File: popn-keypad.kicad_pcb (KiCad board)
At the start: 2 copper layers, 130.9 x 47.6 mm, 14 parts, among them U1 Arduino_Pro_Micro

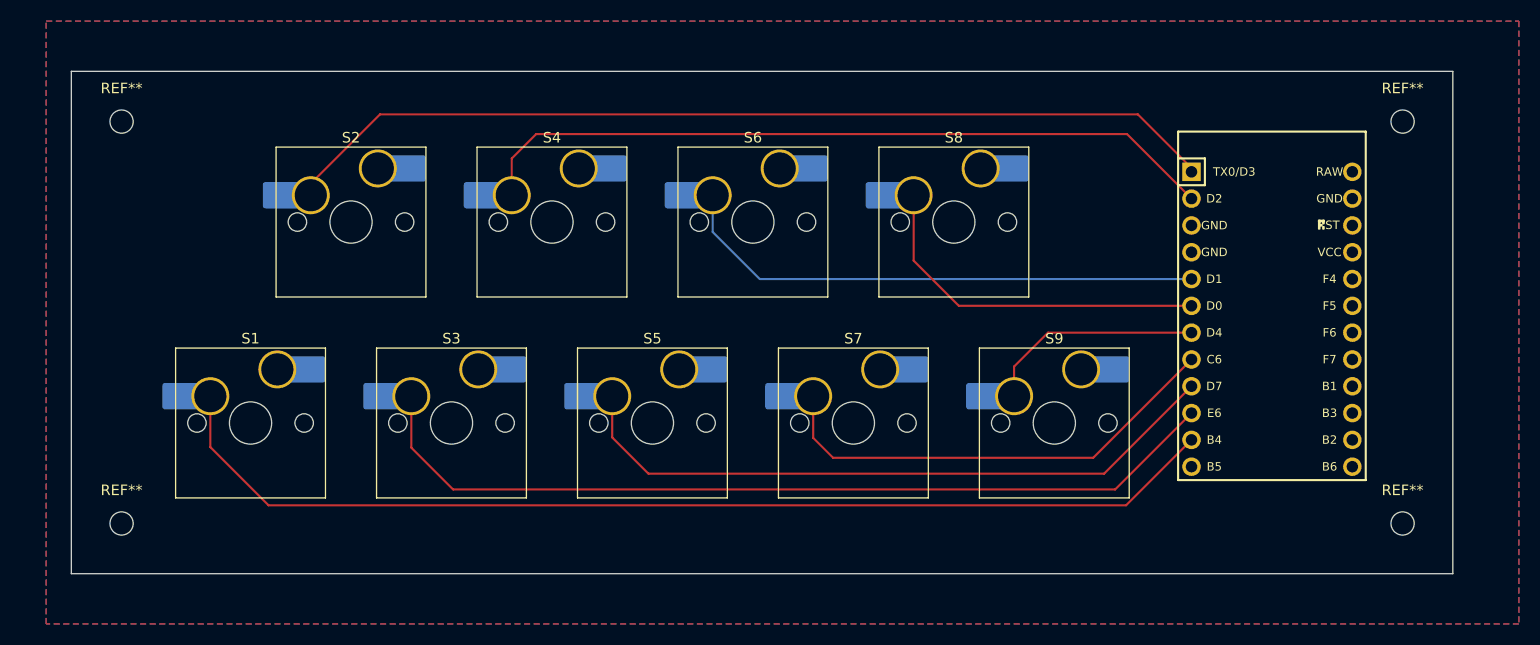
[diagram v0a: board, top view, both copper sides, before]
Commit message: Update popn-keypad.kicad_pcb
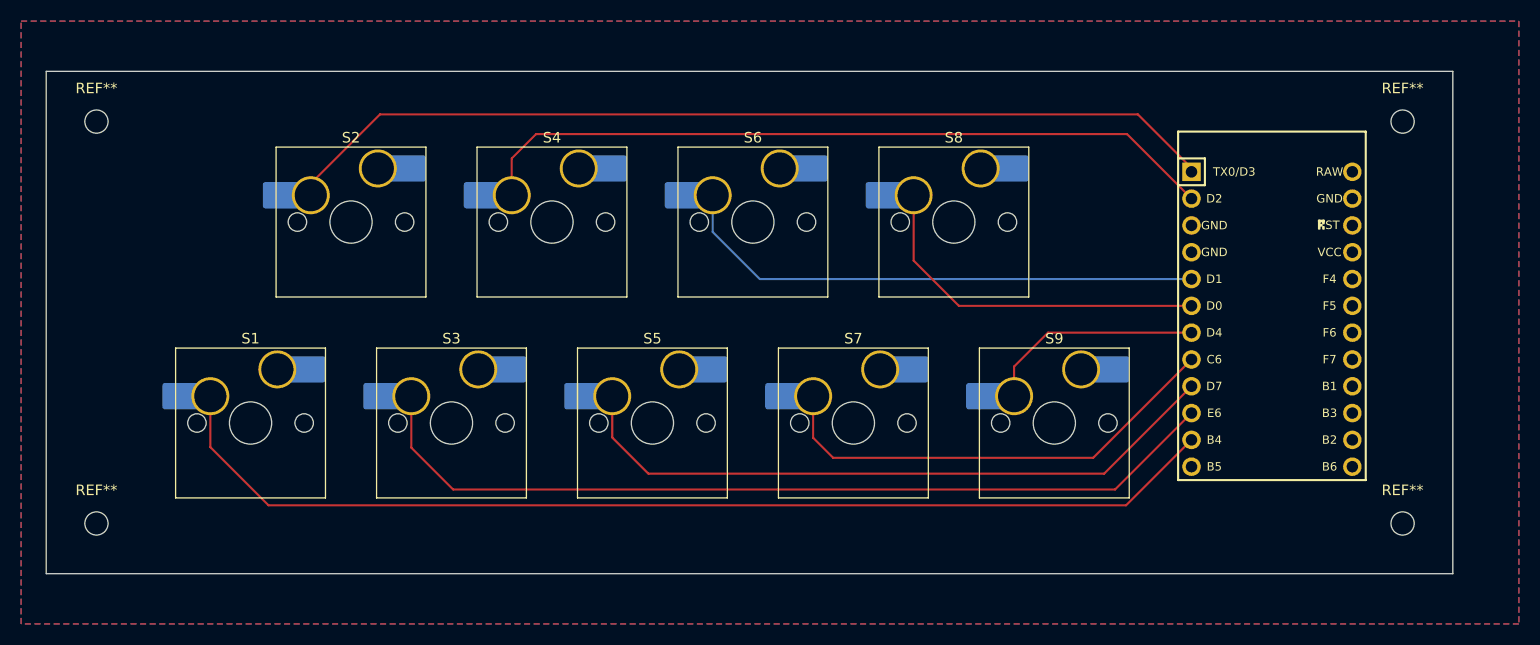
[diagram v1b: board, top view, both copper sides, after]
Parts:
- moved REF** 2.38 mm to (95.2, 104.7)
- moved REF** 2.38 mm to (95.2, 66.6)
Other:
- board size 130.9 x 47.6 mm -> 133.3 x 47.6 mm
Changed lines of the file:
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@@
 	(footprint "MountingHole:MountingHole_2.2mm_M2"
 		(layer "F.Cu")
-		(at 97.58 104.72)
+		(at 95.2 104.72)
 		(descr "Mounting Hole 2.2mm, M2, no annular, generated by kicad-footprint-generator mountinghole.py")
 		(tags "mountinghole M2")
@@
 	(footprint "MountingHole:MountingHole_2.2mm_M2"
 		(layer "F.Cu")
-		(at 97.58 66.64)
+		(at 95.2 66.64)
 		(descr "Mounting Hole 2.2mm, M2, no annular, generated by kicad-footprint-generator mountinghole.py")
 		(tags "mountinghole M2")
@@
 	)
 	(gr_rect
-		(start 92.82 61.88)
+		(start 90.44 61.88)
 		(end 223.72 109.48)
 		(stroke
@@
 		(polygon
 			(pts
-				(xy 90.44 57.12) (xy 229.98 57.12) (xy 229.98 114.24) (xy 90.44 114.24)
+				(xy 88.06 57.12) (xy 229.98 57.12) (xy 229.98 114.24) (xy 88.06 114.24)
 			)
 		)
